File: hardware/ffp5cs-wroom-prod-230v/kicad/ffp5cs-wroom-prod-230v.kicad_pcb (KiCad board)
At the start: 2 copper layers, 166 x 110 mm, 74 parts, among them J1 Bornier_5.08, J10 JST-XH, J11 Bornier_5.08, J12 Bornier_5.08, J13 Support OLED, J14 Support I2C ext, J15 Header servo, J16 Header servo, J17 Header GPIO libres, J18 Bornier_5.08, J19 Bornier_5.08, J2 Jack 5.5/2.1, J20 Header alim, J3 Bornier_5.08, J4 Bornier_5.08, J5 Bornier_5.08, J6 Bornier_5.08, J7 JST-XH, J8 JST-XH, J9 JST-XH, K1 SRD-05VDC-SL-C, K2 SRD-05VDC-SL-C, K3 SRD-05VDC-SL-C, K4 SRD-05VDC-SL-C, Q1 BC337-40, Q2 BC337-40, Q3 BC337-40, Q4 BC337-40

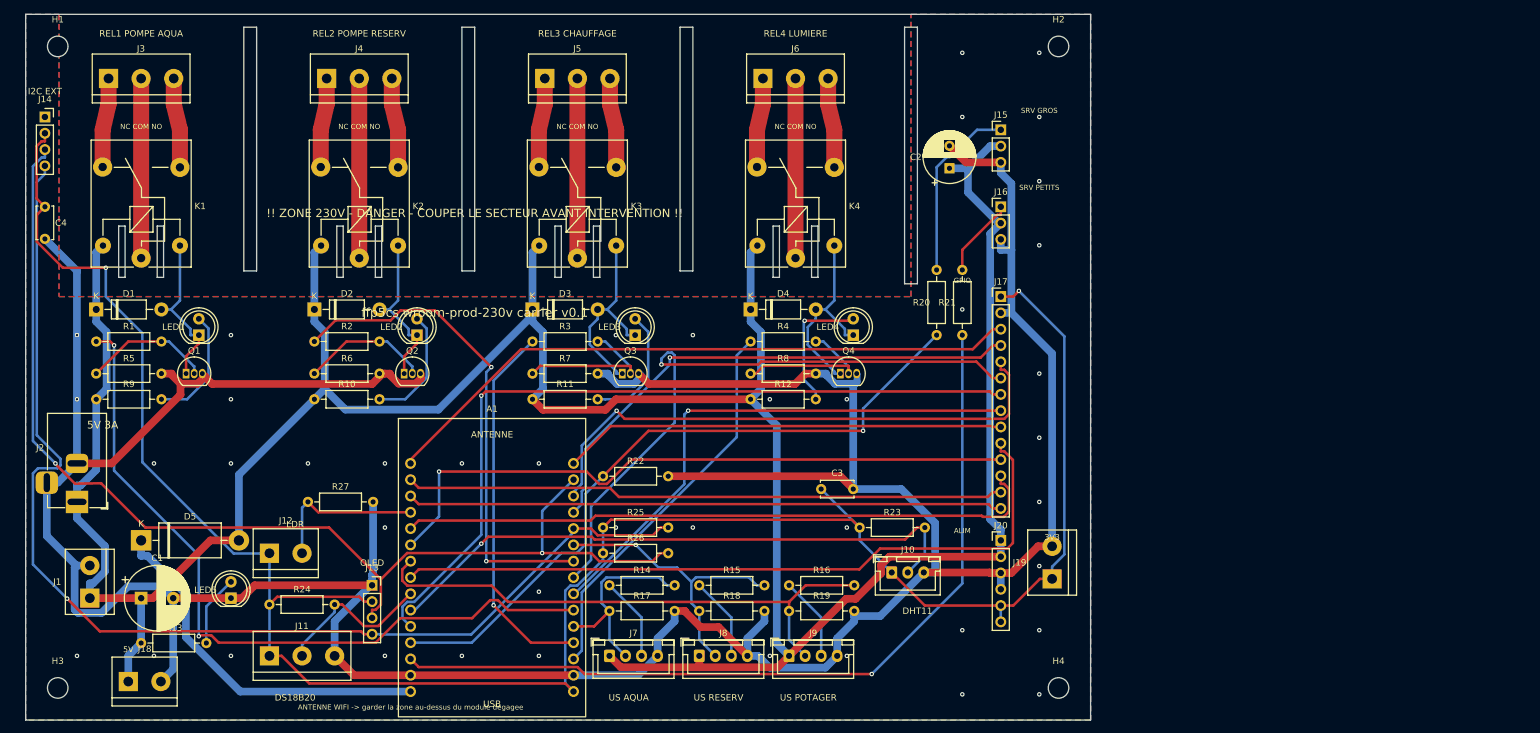
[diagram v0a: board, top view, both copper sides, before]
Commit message: hardware(ffp5cs): 3 ports I2C libres par carte + pipeline de routage LV scripté
Demande : pouvoir brancher des modules I2C supplémentaires sans soudure.
Avec les pull-ups 4.7k en place, 3-4 modules simultanés sont confortables
(limite = capacité du bus, pas l'ESP) — dimensionné en conséquence :

- 12/24V (rev 0.4) : +J18 +J19 (supports 1x4 GND/VCC/SCL/SDA, mêmes nets
  que J14) ; netclasses Relais/Alim désormais émises par generate.py ;
  nouveau generator/route_lv.py (pipeline scripté dérivé de route_230v.py :
  freerouting, vias de couture, îlots supprimés, reliefs corrigés, bandes
  de bord) ; re-routage complet, gerbers v0.4 (remplacent v0.3).
- 230V (rev 0.2) : +J21 +J22 idem ; bandes de keepout le long des bords
  ajoutées au pipeline (l'autorouteur frôlait l'edge clearance) ;
  re-routage complet, gerbers v0.2 (remplacent v0.1).
- Validation des DEUX cartes : ERC 0 erreur, DRC 0 violation, 0 pad non
  connecté, contrôle 3mm secteur/logique (230V) : 0 écart, checker
  pins.h <-> schéma <-> PCB vert.
- READMEs : ports I2C documentés (3-4 modules max, bus < ~50cm, sinon
  pull-ups 2.2k).

Co-Authored-By: Claude Fable 5 <noreply@anthropic.com>
Claude-Session: https://claude.ai/code/session_01HcxShQb65yktRwp31wBq9q
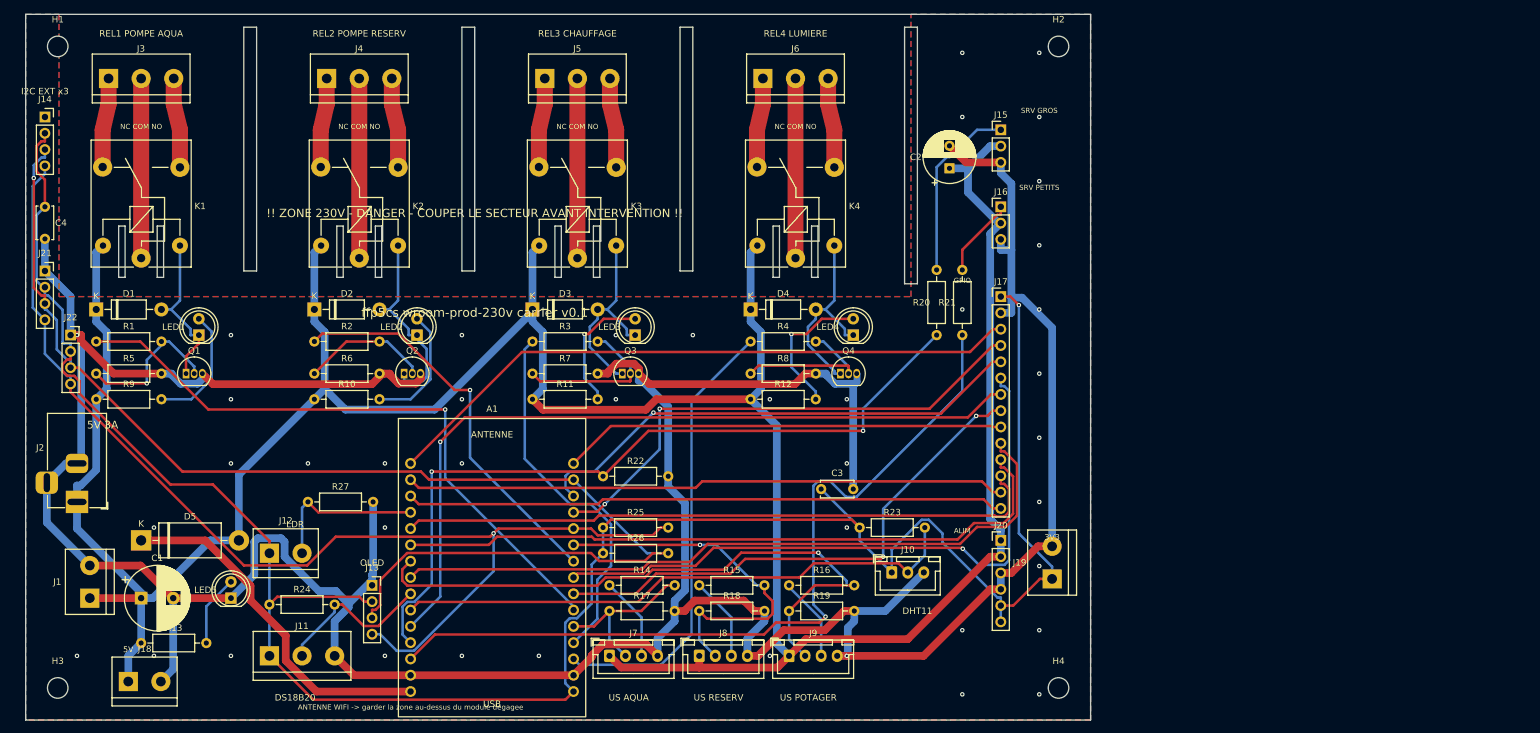
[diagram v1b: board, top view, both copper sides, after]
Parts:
- added J21: Support I2C libre, ffp5cs:PinSocket_1x04_P2.54mm_Vertical, F.Cu at (43.0, 80.0)
- added J22: Support I2C libre, ffp5cs:PinSocket_1x04_P2.54mm_Vertical, F.Cu at (47.0, 90.0)
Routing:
- net I2C_SCL_GPIO22: track 177.7 -> 197.7 mm, vias 2 -> 1
- net PUMP_AQUA_GPIO16: track 116.2 -> 98.3 mm, vias 2 -> 1
- net PUMP_TANK_GPIO18: track 77.4 -> 61.8 mm, vias 2 -> 1
- net US_POTA_GPIO33: track 85.9 -> 98.8 mm, vias 0 -> 1
- net US_TANK_GPIO19: track 46.0 -> 57.6 mm
- net SERVO_GROS_GPIO12: track 108.5 -> 119.9 mm, vias 1 -> 2
- net LIGHT_GPIO15: track 60.9 -> 70.2 mm
- net GND: track 564.9 -> 573.8 mm
- net SPARE_TX0_GPIO1: track 87.1 -> 79.0 mm
- net +3V3: track 343.1 -> 350.9 mm, vias 2 -> 1
- net REL2_SW: track 25.4 -> 30.9 mm
- net US_AQUA_GPIO4: track 31.8 -> 26.4 mm
- net DHT_GPIO27: track 93.9 -> 89.2 mm, vias 1 -> 0
- net REL1_B: track 20.1 -> 24.1 mm, vias 0 -> 1
- net SERVO_PETITS_GPIO13: track 131.5 -> 128.7 mm
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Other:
- board text added: "I2C EXT x3"
- board text removed: "I2C EXT"

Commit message: feat(ffp5cs+hardware): relais AUX1/AUX2 (firmware v15.26, carte 230V 6 canaux) + corrections des 2 cartes
FIRMWARE ffp5cs v15.26 :
- Pins::AUX1/AUX2 (WROOM 23/25, S3 47/48), RelayController generique,
  SystemActuators::setAux/isAuxOn, IActuators::setAux (defaut no-op,
  doubles de test intacts), GPIOMap::AUX1/AUX2 dans ALL_MAPPINGS
  (parser GET + NVS + restauration boot automatiques).
- Garde test_mapping_count_is_stable 27->29 (ajout conscient).
- Tests natifs : 54 suites PASSED ; build wroom-test SUCCESS
  (wroom-prod local refuse par design les secrets placeholder).
- Contrat POST inchange ; cote serveur : n3_serveur 6.38.0 (PR jumelle).

HARDWARE 230V rev 0.3 — 6 canaux (234x110mm) :
- +REL5/REL6 (AUX1/AUX2) : relais+bornier+fentes identiques aux 4 canaux
  metier, refs dediees (R28-R33, D6/D7, LED6/LED7, Q5/Q6, J23/J24).
- J17 breakout 1x14 -> 1x12 (IO23/IO25 ne sont plus des spares).
- Pipeline : bande secteur etendue, min via 0.5, jar freerouting 2.x,
  timeout 1500s. Valide : ERC 0, DRC 0 violation 0 non-connecte,
  controle 3mm secteur/logique 0 ecart, checker 16 signaux vert.
- Gerbers v0.3, fritzing 6 commandes relais, README.

CORRECTIONS COMMUNES (12/24V rev 0.5 + 230V) :
- BOM : ligne 'A1 (supports)' (2 barrettes femelles 1x15) — le DevKit
  est enfichable, jamais soude, mais les supports n'etaient pas commandables.
- Keepout cuivre sous l'antenne WiFi du module (2 faces) + note serigraphiee
  deplacee cote antenne (elle etait sous le corps du module, cote USB).
- Checker etendu a la topologie des canaux HC-SR04 (JST 1=+5V 2=GPIO
  3=ECHO 4=GND ; 1k serie echo ; 2k pull-down) sur les deux cartes.
- 12/24V : pinmap declare AUX1/AUX2 -> spares J17 (modules relais externes) ;
  re-route complet (jar 1.9, le 2.1 depassait le timeout sur cette carte),
  DRC 0/0, gerbers v0.5.

Co-Authored-By: Claude Fable 5 <noreply@anthropic.com>
Claude-Session: https://claude.ai/code/session_01HcxShQb65yktRwp31wBq9q
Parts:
- added D6: 1N4007, ffp5cs:D_DO-41_SOD81_P10.16mm_Horizontal, F.Cu at (187.0, 86.0)
- added D7: 1N4007, ffp5cs:D_DO-41_SOD81_P10.16mm_Horizontal, F.Cu at (221.0, 86.0)
- added J23: Bornier_5.08, ffp5cs:TerminalBlock_bornier-3_P5.08mm, F.Cu at (188.9, 50.0)
- added J24: Bornier_5.08, ffp5cs:TerminalBlock_bornier-3_P5.08mm, F.Cu at (222.9, 50.0)
- added K5: SRD-05VDC-SL-C, ffp5cs:Relay_SPDT_SANYOU_SRD_Series_Form_C, F.Cu at (194.0, 78.0)
- added K6: SRD-05VDC-SL-C, ffp5cs:Relay_SPDT_SANYOU_SRD_Series_Form_C, F.Cu at (228.0, 78.0)
- added LED6: rouge, ffp5cs:LED_D5.0mm, F.Cu at (203.0, 90.0)
- added LED7: rouge, ffp5cs:LED_D5.0mm, F.Cu at (237.0, 90.0)
- added Q5: BC337-40, ffp5cs:TO-92_Inline, F.Cu at (201.0, 96.0)
- added Q6: BC337-40, ffp5cs:TO-92_Inline, F.Cu at (235.0, 96.0)
- added R28: 1k, ffp5cs:R_Axial_DIN0207_L6.3mm_D2.5mm_P10.16mm_Horizontal, F.Cu at (187.0, 91.0)
- added R29: 10k, ffp5cs:R_Axial_DIN0207_L6.3mm_D2.5mm_P10.16mm_Horizontal, F.Cu at (187.0, 96.0)
- added R30: 1k, ffp5cs:R_Axial_DIN0207_L6.3mm_D2.5mm_P10.16mm_Horizontal, F.Cu at (187.0, 100.0)
- added R31: 1k, ffp5cs:R_Axial_DIN0207_L6.3mm_D2.5mm_P10.16mm_Horizontal, F.Cu at (221.0, 91.0)
- added R32: 10k, ffp5cs:R_Axial_DIN0207_L6.3mm_D2.5mm_P10.16mm_Horizontal, F.Cu at (221.0, 96.0)
- added R33: 1k, ffp5cs:R_Axial_DIN0207_L6.3mm_D2.5mm_P10.16mm_Horizontal, F.Cu at (221.0, 100.0)
- J17: footprint ffp5cs:PinHeader_1x14_P2.54mm_Vertical -> ffp5cs:PinHeader_1x12_P2.54mm_Vertical
- moved C2 68.0 mm to (252.0, 64.0)
- moved H2 68.0 mm to (269.0, 45.0)
- moved H4 68.0 mm to (269.0, 145.0)
- moved J15 68.0 mm to (260.0, 58.0)
- moved J16 68.0 mm to (260.0, 70.0)
- moved J17 68.0 mm to (260.0, 84.0)
- moved J19 68.0 mm to (268.0, 128.0)
- moved J20 68.0 mm to (260.0, 122.0)
- moved R20 68.0 mm to (250.0, 90.0)
- moved R21 68.0 mm to (254.0, 90.0)
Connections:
- A1 pad 15: SPARE_GPIO23 -> AUX1_GPIO23
- A1 pad 23: SPARE_GPIO25 -> AUX2_GPIO25
- J17 pad 10: SPARE_GPIO25 -> SPARE_GPIO35
- J17 pad 11: SPARE_GPIO32 -> SPARE_GPIO36
- J17 pad 12: SPARE_GPIO35 -> SPARE_GPIO39
- J17 pad 9: SPARE_GPIO23 -> SPARE_GPIO32
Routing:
- net +5V: track 469.5 -> 664.2 mm, vias 0 -> 2
- net AUX2_GPIO25: track 0.00 -> 161.1 mm, vias 0 -> 3
- net GND: track 573.8 -> 728.7 mm, vias 43 -> 69
- net SPARE_GPIO25: track 111.2 -> 0.00 mm
- net SPARE_GPIO35: track 100.9 -> 200.6 mm, vias 0 -> 3
- net EN: track 100.7 -> 179.6 mm, vias 0 -> 1
- net SPARE_GPIO36: track 93.6 -> 172.6 mm, vias 0 -> 1
- net SPARE_GPIO17: track 82.8 -> 158.3 mm
- net SPARE_TX0_GPIO1: track 79.0 -> 154.1 mm
- net SPARE_RX0_GPIO3: track 81.1 -> 156.0 mm, vias 2 -> 1
- net SPARE_GPIO32: track 105.8 -> 180.4 mm, vias 0 -> 1
- net AUX1_GPIO23: track 0.00 -> 73.7 mm, vias 0 -> 1
- net SPARE_GPIO39: track 93.4 -> 162.6 mm
- net SPARE_GPIO23: track 69.1 -> 0.00 mm
- net SERVO_PETITS_GPIO13: track 128.7 -> 196.4 mm
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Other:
- board size 166 x 110 mm -> 234 x 110 mm
- board text added: "ANTENNE WIFI : zone degagee (pas de cuivre dessous)"
- board text added: "REL5 AUX1"
- board text added: "REL6 AUX2"
- board text added: "ffp5cs wroom-prod-230v carrier v0.3 (6 canaux)"
- board text removed: "ANTENNE WIFI -> garder la zone au-dessus du module degagee"
- board text removed: "ffp5cs wroom-prod-230v carrier v0.1"

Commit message: fix(hardware): fichiers de fabrication et sérigraphie prêts pour JLCPCB
Trois défauts trouvés en préparant une commande, sur les 3 cartes :

1. Sérigraphie sous les minima fabricant : textes de 0,8 mm de haut / 0,12 mm
   de trait, alors que JLCPCB exige 1 mm / 0,15 mm — les étiquettes de câblage
   (NO COM NC, ADC A 33, ZONE 230V - DANGER...) risquaient d'être floutées ou
   supprimées par leur DFM. Tous les textes passent à >= 1 mm / 0,16 mm.
2. Repères de composants superposés aux étiquettes (34 chevauchements, dont
   l'avertissement 230 V masqué par K3/K4). Nouveau generator/tidy_silkscreen.py :
   écarte le repère (court, recasable) sans jamais bouger l'étiquette dont la
   position porte le sens. Déterministe, idempotent, avec audit final par couche.
   Titre de la carte 12/24 V déplacé (il croisait REL2/REL3).
3. Zip Gerbers de la carte commune pollué par 6 couches de documentation
   (F.Fab, *.Courtyard, User.*, Margin) et perçages PTH/NPTH fusionnés.
   Nouveau generator/export_fab.py : exactement les 7 couches utiles + PTH/NPTH
   séparés (trous M3 non métallisés) + rendus de revue sans cartouche de page.
   Aucun script d'export n'existait dans le dépôt — les exports n'étaient pas
   reproductibles, d'où la divergence entre cartes.

Ajouts : marqueur JLCJLCJLCJLC au dos des 3 cartes (emplacement du numéro de
commande imposé au fabricant, gratuit, plutôt qu'au hasard sur une étiquette),
et hardware/COMMANDE_JLCPCB.md — réglages du formulaire expliqués un par un,
choix par carte (1 oz vs 2 oz pour le 230 V, confirmation des fentes fraisées).

Cuivre inchangé : DRC 0 violation / 0 pastille non connectée sur les 3 cartes,
règle .kicad_dru 3 mm secteur toujours vérifiée sur la carte 230 V.

Co-Authored-By: Claude Opus 5 <noreply@anthropic.com>
Claude-Session: https://claude.ai/code/session_01HcxShQb65yktRwp31wBq9q
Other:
- board text added: "JLCJLCJLCJLC"
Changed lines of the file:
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@@
 		(tags "Through hole socket strip THT 1x04 2.54mm single row")
 		(property "Reference" "J13"
-			(at 0 -2.77 0)
+			(at 0 -1.77 0)
 			(layer "F.SilkS")
 			(effects
@@
 		(tags "ESP32 DevKit V1")
 		(property "Reference" "A1"
-			(at 12.7 -8.5 0)
+			(at 12.7 -10.5 0)
 			(layer "F.SilkS")
 			(effects
@@
 		(tags "terminal block bornier2")
 		(property "Reference" "J12"
-			(at 2.54 -5.08 0)
+			(at 2.54 -6.58 0)
 			(layer "F.SilkS")
 			(effects
@@
 		(tags "terminal block bornier2")
 		(property "Reference" "J18"
-			(at 2.54 -5.08 0)
+			(at 2.54 -4.08 0)
 			(layer "F.SilkS")
 			(effects
@@
 		(tags "Through hole socket strip THT 1x04 2.54mm single row")
 		(property "Reference" "J14"
-			(at 0 -2.77 0)
+			(at 0 -2.27 0)
 			(layer "F.SilkS")
 			(effects
@@
 		(tags "relay Sanyu SRD form C")
 		(property "Reference" "K4"
-			(at 8.1 9.2 0)
+			(at 9.1 9.2 0)
 			(layer "F.SilkS")
 			(effects
@@
 		(tags "relay Sanyu SRD form C")
 		(property "Reference" "K3"
-			(at 8.1 9.2 0)
+			(at 9.1 9.2 0)
 			(layer "F.SilkS")
 			(effects
@@
 		(layer "Edge.Cuts")
 	)
+	(gr_text "JLCJLCJLCJLC"
+		(at 80 145.5 0)
+		(layer "B.SilkS")
+		(effects
+			(font
+				(size 1 1)
+				(thickness 0.16)
+			)
+			(justify mirror)
+		)
+	)
 	(gr_text "ffp5cs wroom-prod-230v carrier v0.3 (6 canaux)"
 		(at 110 86.5 0)
@@
 			(font
 				(size 1.4 1.4)
-				(thickness 0.21)
+				(thickness 0.22)
 			)
 		)
@@
 			(font
 				(size 1 1)
-				(thickness 0.15)
+				(thickness 0.16)
 			)
 		)
@@
 			(font
 				(size 1.2 1.2)
-				(thickness 0.18)
+				(thickness 0.19)
 			)
 		)
@@
 			(font
 				(size 1 1)
-				(thickness 0.15)
+				(thickness 0.16)
 			)
 		)
@@
 			(font
 				(size 1.3 1.3)
-				(thickness 0.2)
+				(thickness 0.21)
 			)
 		)
@@
 			(font
 				(size 1 1)
-				(thickness 0.15)
+				(thickness 0.16)
 			)
 		)
@@
 		(effects
 			(font
-				(size 0.9 0.9)
-				(thickness 0.14)
+				(size 1 1)
+				(thickness 0.16)
 			)
 		)
@@
 			(font
 				(size 1 1)
-				(thickness 0.15)
+				(thickness 0.16)
 			)
 		)
@@
 			(font
 				(size 1 1)
-				(thickness 0.15)
+				(thickness 0.16)
 			)
 		)
@@
 			(font
 				(size 1 1)
-				(thickness 0.15)
+				(thickness 0.16)
 			)
 		)
@@
 		(effects
 			(font
-				(size 0.8 0.8)
-				(thickness 0.12)
+				(size 1 1)
+				(thickness 0.16)
 			)
 		)
@@
 			(font
 				(size 1 1)
-				(thickness 0.15)
+				(thickness 0.16)
 			)
 		)
@@
 		(effects
 			(font
-				(size 0.8 0.8)
-				(thickness 0.12)
+				(size 1 1)
+				(thickness 0.16)
 			)
 		)
@@
 			(font
 				(size 1 1)
-				(thickness 0.15)
+				(thickness 0.16)
 			)
 		)
@@
 			(font
 				(size 1 1)
-				(thickness 0.15)
+				(thickness 0.16)
 			)
 		)
@@
 			(font
 				(size 1 1)
-				(thickness 0.15)
+				(thickness 0.16)
 			)
 		)
@@
 		(effects
 			(font
-				(size 0.8 0.8)
-				(thickness 0.12)
+				(size 1 1)
+				(thickness 0.16)
 			)
 		)
@@
 			(font
 				(size 1 1)
-				(thickness 0.15)
+				(thickness 0.16)
 			)
 		)
@@
 		(effects
 			(font
-				(size 0.8 0.8)
-				(thickness 0.12)
+				(size 1 1)
+				(thickness 0.16)
 			)
 		)
@@
 		(effects
 			(font
-				(size 0.8 0.8)
-				(thickness 0.12)
+				(size 1 1)
+				(thickness 0.16)
 			)
 		)
@@
 			(font
 				(size 1 1)
-				(thickness 0.15)
+				(thickness 0.16)
 			)
 		)
@@
 		(effects
 			(font
-				(size 0.8 0.8)
-				(thickness 0.12)
+				(size 1 1)
+				(thickness 0.16)
 			)
 		)
@@
 		(effects
 			(font
-				(size 0.8 0.8)
-				(thickness 0.12)
+				(size 1 1)
+				(thickness 0.16)
 			)
 		)
@@
 		(effects
 			(font
-				(size 0.8 0.8)
-				(thickness 0.12)
+				(size 1 1)
+				(thickness 0.16)
 			)
 		)
@@
 		(effects
 			(font
-				(size 0.8 0.8)
-				(thickness 0.12)
+				(size 1 1)
+				(thickness 0.16)
 			)
 		)
@@
 		(effects
 			(font
-				(size 0.8 0.8)
-				(thickness 0.12)
+				(size 1 1)
+				(thickness 0.16)
 			)
 		)
@@
 		(effects
 			(font
-				(size 0.8 0.8)
-				(thickness 0.12)
+				(size 1 1)
+				(thickness 0.16)
 			)
 		)
@@
 			(font
 				(size 1 1)
-				(thickness 0.15)
+				(thickness 0.16)
 			)
 		)
@@
 		(effects
 			(font
-				(size 0.9 0.9)
-				(thickness 0.14)
+				(size 1 1)
+				(thickness 0.16)
 			)
 		)
@@
 			(font
 				(size 1 1)
-				(thickness 0.15)
+				(thickness 0.16)
 			)
 		)
